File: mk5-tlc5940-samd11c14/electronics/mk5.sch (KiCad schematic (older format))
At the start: 47 parts, among them J1 IN/OUT, J10 Conn_01x01, J11 Conn_01x01, J12 Conn_01x01, J13 Conn_01x01, J14 Conn_01x01, J15 Conn_01x01, J16 Conn_01x01, J17 Conn_01x01, J18 Conn_01x01, J19 Conn_01x01, J2 USB, J20 Conn_01x01, J21 Conn_01x01, J22 Conn_01x01, J23 +LED, J24 +LED, J25 +LED, J26 +LED, J27 +LED, J3 OUT15, J4 GS2, J5 BUTTON, J6 +LED, J7 Conn_01x01, J8 Conn_01x01, J9 Conn_01x01, Q1 MOSFET 20V 3A, SW1 BTN, U1 USBLC6-2SC6, U2 MCP1702-3302_SOT23, U3 SAMD11D14A-M, U4 TLC5940PWP

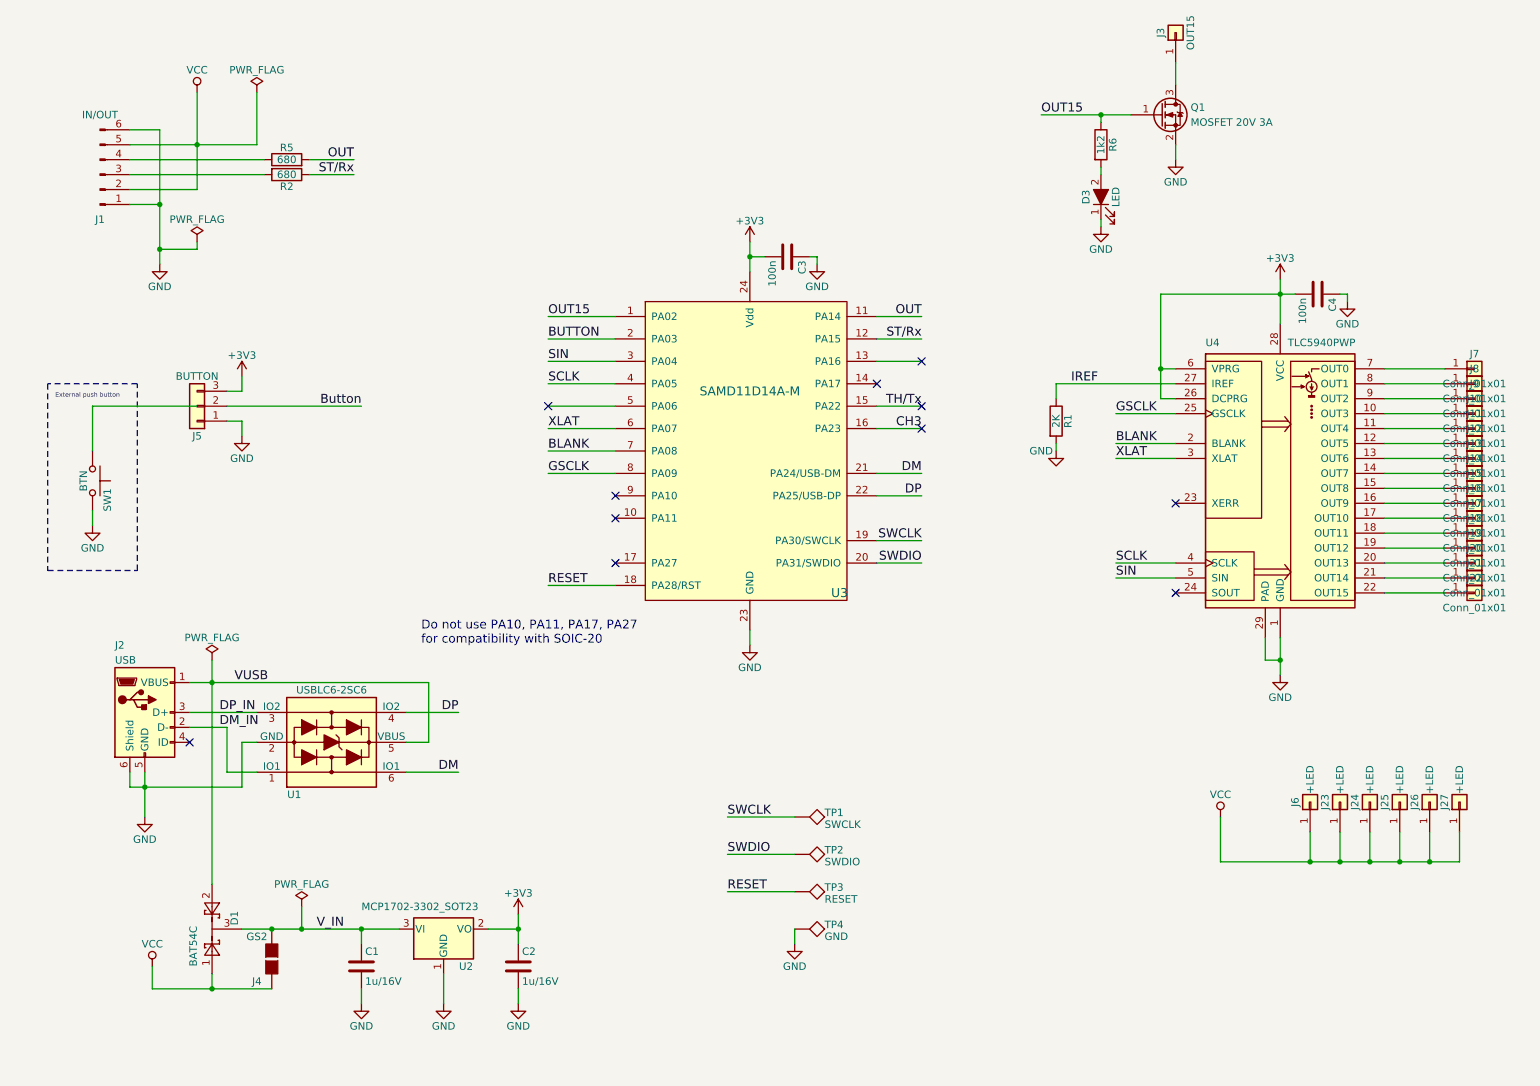
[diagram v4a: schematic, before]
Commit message: Finalize layout with reverse-mount LED
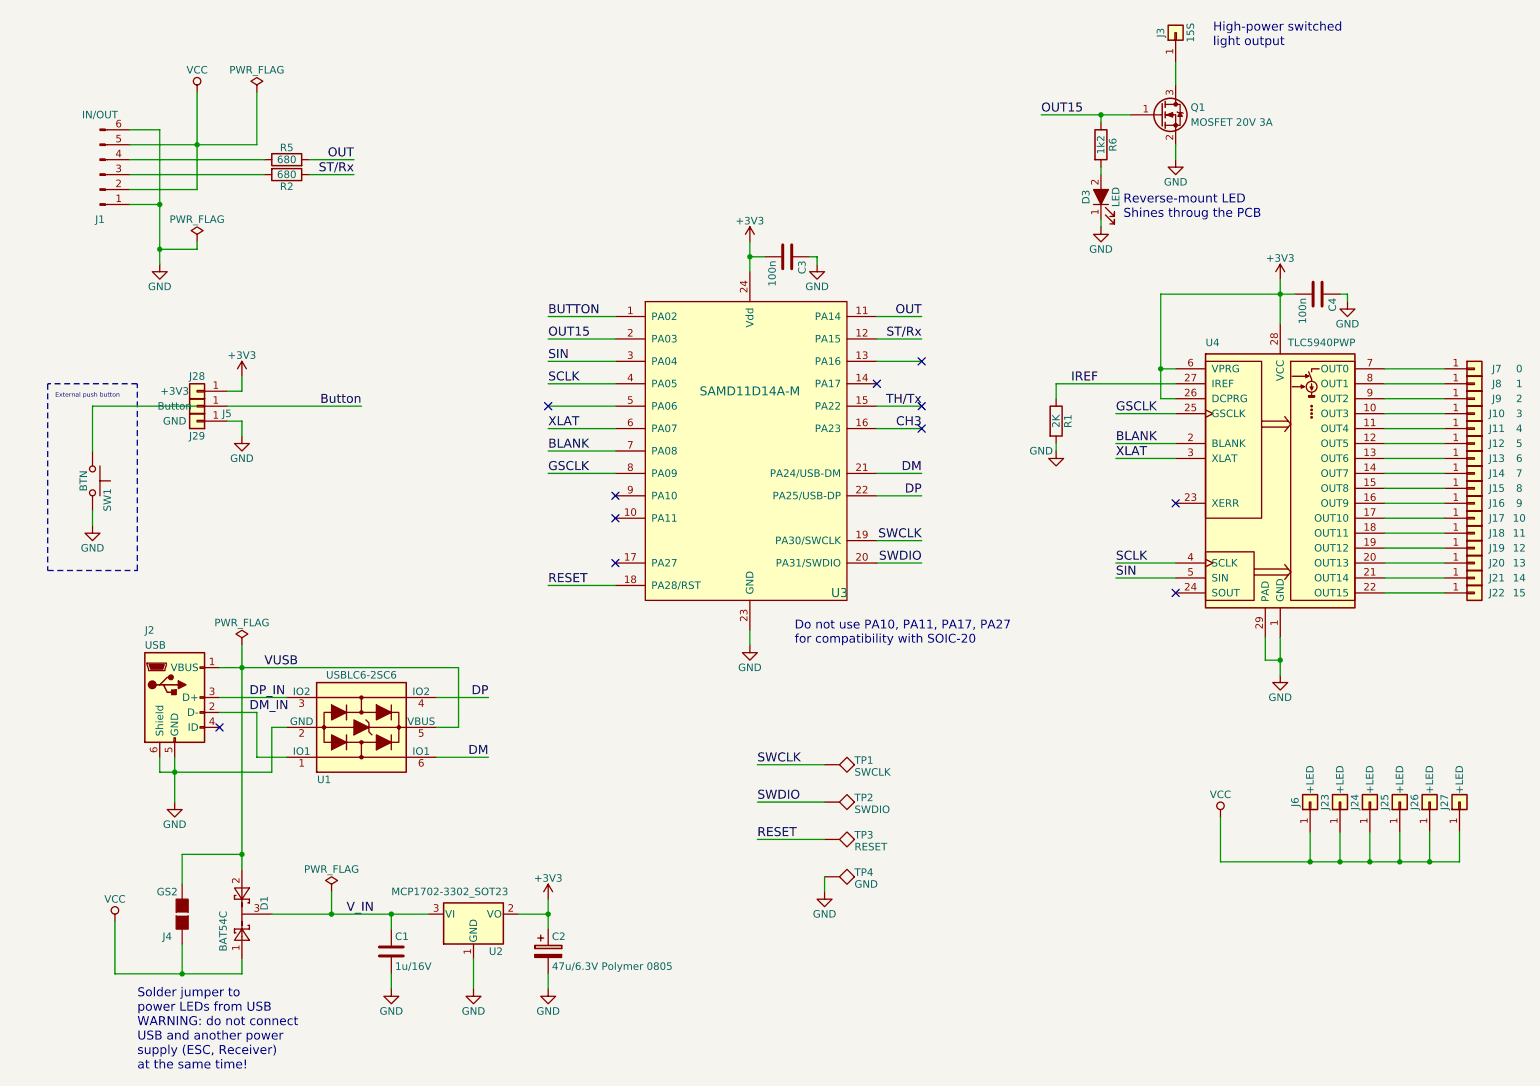
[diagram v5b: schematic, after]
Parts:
- removed C2: 1u/16V, Capacitors_SMD:C_0805, symbol C
- removed J5: BUTTON, Socket_Strips:Socket_Strip_Straight_1x03, symbol Conn_01x03
- added C2: 47u/6.3V Polymer 0805, Capacitors_SMD:C_0805, symbol CP
- added J28: Button, Measurement_Points:Measurement_Point_Round-SMD-Pad_Small, symbol Conn_01x01
- added J29: GND, Measurement_Points:Measurement_Point_Round-SMD-Pad_Small, symbol Conn_01x01
- added J5: +3V3, Measurement_Points:Measurement_Point_Round-SMD-Pad_Small, symbol Conn_01x01
- D3: footprint LEDs:LED_0805_HandSoldering -> Reverse-LED:REVERSE_MOUNT_ROHM_SLM-81
- J10: value Conn_01x01 -> 3
- J11: value Conn_01x01 -> 4
- J12: value Conn_01x01 -> 5
- J13: value Conn_01x01 -> 6
- J14: value Conn_01x01 -> 7
- J15: value Conn_01x01 -> 8
- J16: value Conn_01x01 -> 9
- J17: value Conn_01x01 -> 10
- J18: value Conn_01x01 -> 11
- J19: value Conn_01x01 -> 12
- J20: value Conn_01x01 -> 13
- J21: value Conn_01x01 -> 14
- J22: value Conn_01x01 -> 15
- J3: value OUT15 -> 15S
- J7: value Conn_01x01 -> 0
- J8: value Conn_01x01 -> 1
- J9: value Conn_01x01 -> 2
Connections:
- net +3V3: now also C2.1, J5.1 (Pin_1)
- net BUTTON: now also U3.1 (PA02); no longer U3.2 (PA03)
- net Button: now also J28.1 (Pin_1)
- net GND: now also C2.2, J29.1 (Pin_1)
- net OUT15: now also U3.2 (PA03); no longer U3.1 (PA02)
- net VUSB: now also J4.2 (G2)
- net V_IN: no longer J4.2 (G2)
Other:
- note added: "High-power switched\nlight output"
- note added: "Reverse-mount LED\nShines throug the PCB"
- note added: "Solder jumper to\npower LEDs from USB\nWARNING: do not connect\nUSB and another power \nsupply (ESC, Receiver) \nat the same time!"
- moved on the sheet: C1, D1, J2, J4, TP1, TP2, TP3, TP4, U1, U2

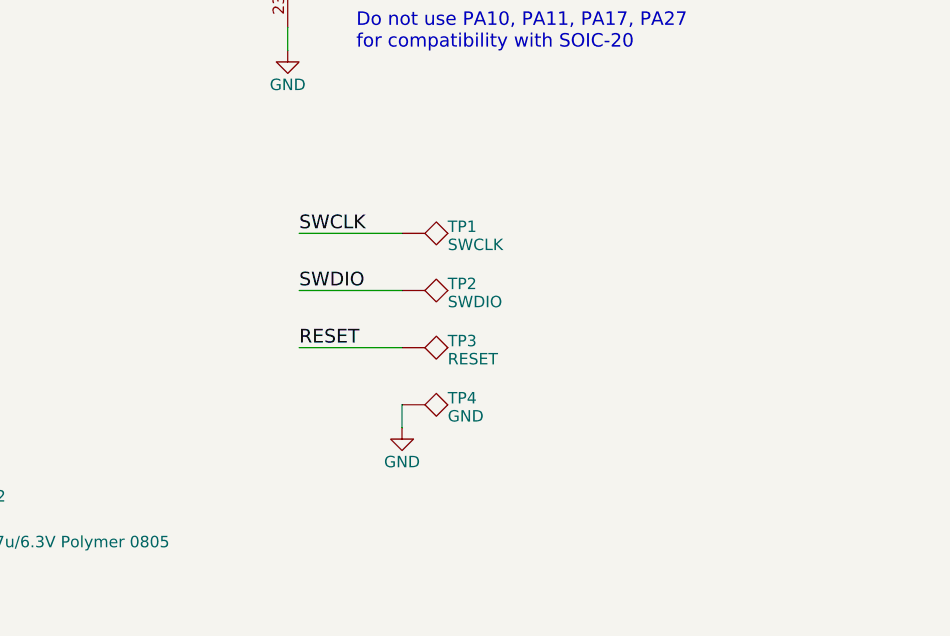
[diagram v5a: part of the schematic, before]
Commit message: Add test points
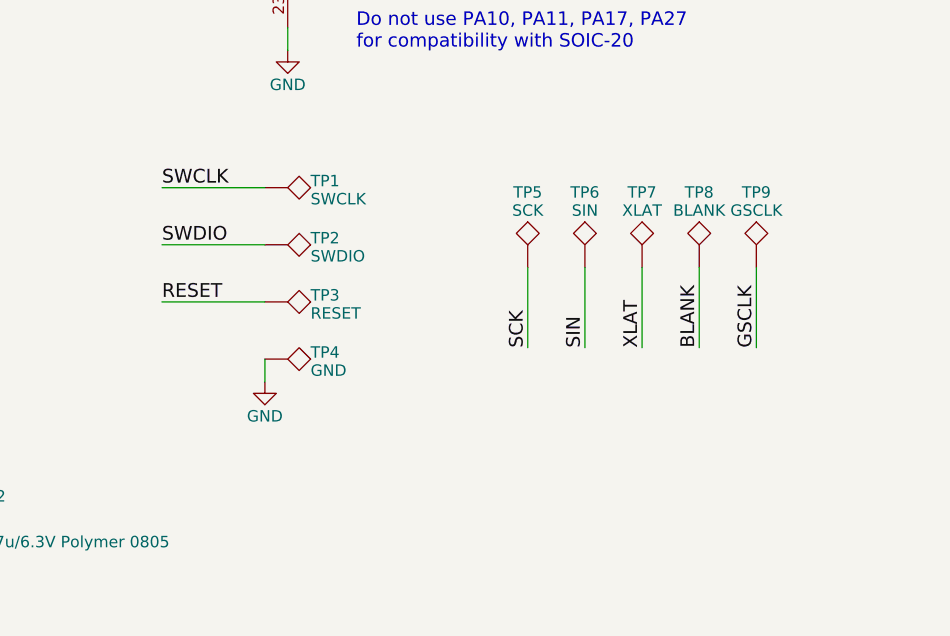
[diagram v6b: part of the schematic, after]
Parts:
- added TP5: SCK, SMD-pads:Measurement_Point_Round-SMD-Pad_1mm, symbol TEST
- added TP6: SIN, SMD-pads:Measurement_Point_Round-SMD-Pad_1mm, symbol TEST
- added TP7: XLAT, SMD-pads:Measurement_Point_Round-SMD-Pad_1mm, symbol TEST
- added TP8: BLANK, SMD-pads:Measurement_Point_Round-SMD-Pad_1mm, symbol TEST
- added TP9: GSCLK, SMD-pads:Measurement_Point_Round-SMD-Pad_1mm, symbol TEST
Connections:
- net BLANK: now also TP8.1
- net GSCLK: now also TP9.1
- net SIN: now also TP6.1
- net XLAT: now also TP7.1
- new net SCK: TP5.1
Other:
- moved on the sheet: TP1, TP2, TP3, TP4
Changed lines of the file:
@@
 L TEST TP1
 U 1 1 59C46169
-P 6200 5600
-F 0 "TP1" V 6200 5800 50  0000 L BNN
-F 1 "SWCLK" V 6250 5800 50  0000 L CNN
-F 2 "Measurement_Points:Measurement_Point_Round-SMD-Pad_Small" H 6200 5600 50  0001 C CNN
-F 3 "" H 6200 5600 50  0001 C CNN
-	1    6200 5600
+P 5600 5400
+F 0 "TP1" V 5600 5600 50  0000 L BNN
+F 1 "SWCLK" V 5650 5600 50  0000 L CNN
+F 2 "Measurement_Points:Measurement_Point_Round-SMD-Pad_Small" H 5600 5400 50  0001 C CNN
+F 3 "" H 5600 5400 50  0001 C CNN
+	1    5600 5400
 	0    1    1    0
 $EndComp
@@
 L TEST TP2
 U 1 1 59C46225
-P 6200 5850
-F 0 "TP2" V 6200 6050 50  0000 L BNN
-F 1 "SWDIO" V 6250 6050 50  0000 L CNN
-F 2 "Measurement_Points:Measurement_Point_Round-SMD-Pad_Small" H 6200 5850 50  0001 C CNN
-F 3 "" H 6200 5850 50  0001 C CNN
-	1    6200 5850
+P 5600 5650
+F 0 "TP2" V 5600 5850 50  0000 L BNN
+F 1 "SWDIO" V 5650 5850 50  0000 L CNN
+F 2 "Measurement_Points:Measurement_Point_Round-SMD-Pad_Small" H 5600 5650 50  0001 C CNN
+F 3 "" H 5600 5650 50  0001 C CNN
+	1    5600 5650
 	0    1    1    0
 $EndComp
@@
 L TEST TP3
 U 1 1 59C4652D
-P 6200 6100
-F 0 "TP3" V 6200 6300 50  0000 L BNN
-F 1 "RESET" V 6250 6300 50  0000 L CNN
-F 2 "Measurement_Points:Measurement_Point_Round-SMD-Pad_Small" H 6200 6100 50  0001 C CNN
-F 3 "" H 6200 6100 50  0001 C CNN
-	1    6200 6100
+P 5600 5900
+F 0 "TP3" V 5600 6100 50  0000 L BNN
+F 1 "RESET" V 5650 6100 50  0000 L CNN
+F 2 "Measurement_Points:Measurement_Point_Round-SMD-Pad_Small" H 5600 5900 50  0001 C CNN
+F 3 "" H 5600 5900 50  0001 C CNN
+	1    5600 5900
 	0    1    1    0
 $EndComp
@@
 L TEST TP4
 U 1 1 59DB5CFC
-P 6200 6350
-F 0 "TP4" V 6200 6550 50  0000 L BNN
-F 1 "GND" V 6250 6550 50  0000 L CNN
-F 2 "Measurement_Points:Measurement_Point_Round-SMD-Pad_Small" H 6200 6350 50  0001 C CNN
-F 3 "" H 6200 6350 50  0001 C CNN
-	1    6200 6350
+P 5600 6150
+F 0 "TP4" V 5600 6350 50  0000 L BNN
+F 1 "GND" V 5650 6350 50  0000 L CNN
+F 2 "Measurement_Points:Measurement_Point_Round-SMD-Pad_Small" H 5600 6150 50  0001 C CNN
+F 3 "" H 5600 6150 50  0001 C CNN
+	1    5600 6150
 	0    1    1    0
 $EndComp
@@
 L GND #PWR022
 U 1 1 59DB5EB3
-P 6200 6450
-F 0 "#PWR022" H 6200 6200 50  0001 C CNN
-F 1 "GND" H 6200 6300 50  0000 C CNN
-F 2 "" H 6200 6450 50  0001 C CNN
-F 3 "" H 6200 6450 50  0001 C CNN
-	1    6200 6450
+P 5600 6250
+F 0 "#PWR022" H 5600 6000 50  0001 C CNN
+F 1 "GND" H 5600 6100 50  0000 C CNN
+F 2 "" H 5600 6250 50  0001 C CNN
+F 3 "" H 5600 6250 50  0001 C CNN
+	1    5600 6250
 	1    0    0    -1
 $EndComp
@@
 Text Label 6850 4250 2    60   ~ 0
 SWDIO
-Text Label 5750 5600 0    60   ~ 0
+Text Label 5150 5400 0    60   ~ 0
 SWCLK
-Text Label 5750 5850 0    60   ~ 0
+Text Label 5150 5650 0    60   ~ 0
 SWDIO
-Text Label 5750 6100 0    60   ~ 0
+Text Label 5150 5900 0    60   ~ 0
 RESET
 Text Label 4350 4400 0    60   ~ 0
@@
 Connection ~ 10250 6250
 Wire Wire Line
-	6200 6350 6200 6450
+	5600 6150 5600 6250
 Wire Wire Line
 	1550 1350 1750 1350
@@
 	7750 3050 7750 3150
 Wire Wire Line
-	6200 5600 5750 5600
-Wire Wire Line
-	6200 5850 5750 5850
-Wire Wire Line
-	6200 6100 5750 6100
+	5600 5400 5150 5400
+Wire Wire Line
+	5600 5650 5150 5650
+Wire Wire Line
+	5600 5900 5150 5900
 Wire Wire Line
 	8050 1300 8050 1250
@@
 Text Notes 1600 7650 0    60   ~ 0
 Solder jumper to\npower LEDs from USB\nWARNING: do not connect\nUSB and another power \nsupply (ESC, Receiver) \nat the same time!
+$Comp
+L TEST TP6
+U 1 1 5A12668E
+P 7000 5750
+F 0 "TP6" H 7000 6050 50  0000 C BNN
+F 1 "SIN" H 7000 6000 50  0000 C CNN
+F 2 "SMD-pads:Measurement_Point_Round-SMD-Pad_1mm" H 7000 5750 50  0001 C CNN
+F 3 "" H 7000 5750 50  0001 C CNN
+	1    7000 5750
+	1    0    0    -1
+$EndComp
+$Comp
+L TEST TP7
+U 1 1 5A1272F3
+P 7250 5750
+F 0 "TP7" H 7250 6050 50  0000 C BNN
+F 1 "XLAT" H 7250 6000 50  0000 C CNN
+F 2 "SMD-pads:Measurement_Point_Round-SMD-Pad_1mm" H 7250 5750 50  0001 C CNN
+F 3 "" H 7250 5750 50  0001 C CNN
+	1    7250 5750
+	1    0    0    -1
+$EndComp
+$Comp
+L TEST TP8
+U 1 1 5A1273A0
+P 7500 5750
+F 0 "TP8" H 7500 6050 50  0000 C BNN
+F 1 "BLANK" H 7500 6000 50  0000 C CNN
+F 2 "SMD-pads:Measurement_Point_Round-SMD-Pad_1mm" H 7500 5750 50  0001 C CNN
+F 3 "" H 7500 5750 50  0001 C CNN
+	1    7500 5750
+	1    0    0    -1
+$EndComp
+$Comp
+L TEST TP9
+U 1 1 5A127450
+P 7750 5750
+F 0 "TP9" H 7750 6050 50  0000 C BNN
+F 1 "GSCLK" H 7750 6000 50  0000 C CNN
+F 2 "SMD-pads:Measurement_Point_Round-SMD-Pad_1mm" H 7750 5750 50  0001 C CNN
+F 3 "" H 7750 5750 50  0001 C CNN
+	1    7750 5750
+	1    0    0    -1
+$EndComp
+$Comp
+L TEST TP5
+U 1 1 5A12767F
+P 6750 5750
+F 0 "TP5" H 6750 6050 50  0000 C BNN
+F 1 "SCK" H 6750 6000 50  0000 C CNN
+F 2 "SMD-pads:Measurement_Point_Round-SMD-Pad_1mm" H 6750 5750 50  0001 C CNN
+F 3 "" H 6750 5750 50  0001 C CNN
+	1    6750 5750
+	1    0    0    -1
+$EndComp
+Wire Wire Line
+	6750 5750 6750 6100
+Wire Wire Line
+	7000 5750 7000 6100
+Wire Wire Line
+	7250 5750 7250 6100
+Wire Wire Line
+	7500 5750 7500 6100
+Wire Wire Line
+	7750 5750 7750 6100
+Text Label 6750 6100 1    60   ~ 0
+SCK
+Text Label 7000 6100 1    60   ~ 0
+SIN
+Text Label 7250 6100 1    60   ~ 0
+XLAT
+Text Label 7500 6100 1    60   ~ 0
+BLANK
+Text Label 7750 6100 1    60   ~ 0
+GSCLK
 $EndSCHEMATC

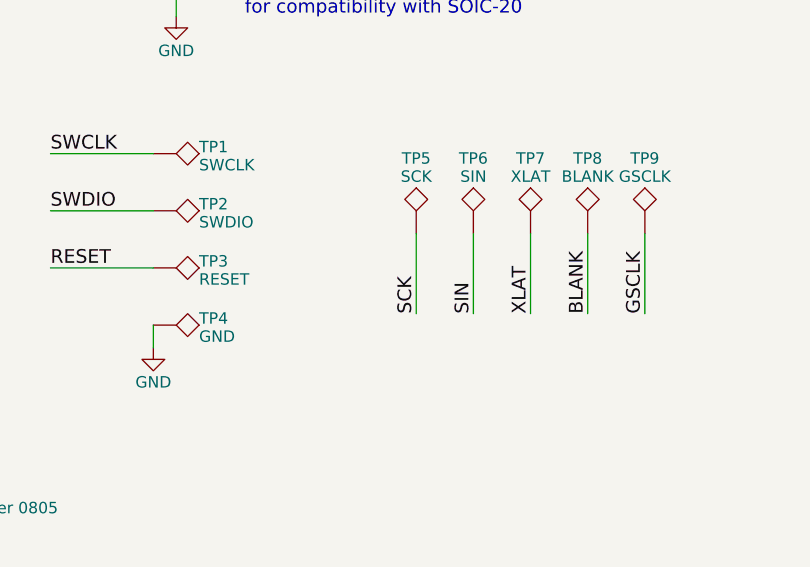
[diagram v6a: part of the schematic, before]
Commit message: Layout test points and tweak
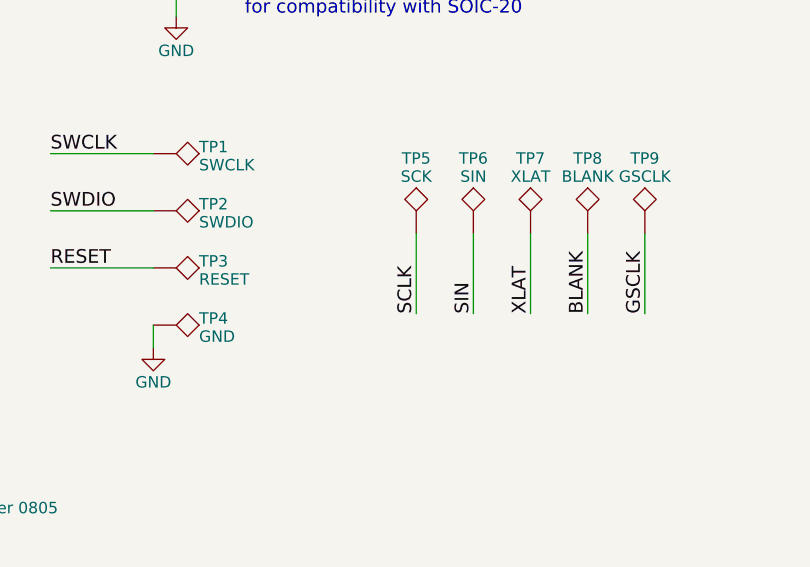
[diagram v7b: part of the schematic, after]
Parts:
- TP5, TP6, TP7, TP8, TP9: footprint SMD-pads:Measurement_Point_Round-SMD-Pad_1mm -> SMD-pads:Measurement_Point_Round-SMD-Pad_0_6mm
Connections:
- net SCK is gone; now on net SCLK: TP5.1
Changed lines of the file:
@@
 F 0 "TP6" H 7000 6050 50  0000 C BNN
 F 1 "SIN" H 7000 6000 50  0000 C CNN
-F 2 "SMD-pads:Measurement_Point_Round-SMD-Pad_1mm" H 7000 5750 50  0001 C CNN
+F 2 "SMD-pads:Measurement_Point_Round-SMD-Pad_0_6mm" H 7000 5750 50  0001 C CNN
 F 3 "" H 7000 5750 50  0001 C CNN
 	1    7000 5750
@@
 F 0 "TP7" H 7250 6050 50  0000 C BNN
 F 1 "XLAT" H 7250 6000 50  0000 C CNN
-F 2 "SMD-pads:Measurement_Point_Round-SMD-Pad_1mm" H 7250 5750 50  0001 C CNN
+F 2 "SMD-pads:Measurement_Point_Round-SMD-Pad_0_6mm" H 7250 5750 50  0001 C CNN
 F 3 "" H 7250 5750 50  0001 C CNN
 	1    7250 5750
@@
 F 0 "TP8" H 7500 6050 50  0000 C BNN
 F 1 "BLANK" H 7500 6000 50  0000 C CNN
-F 2 "SMD-pads:Measurement_Point_Round-SMD-Pad_1mm" H 7500 5750 50  0001 C CNN
+F 2 "SMD-pads:Measurement_Point_Round-SMD-Pad_0_6mm" H 7500 5750 50  0001 C CNN
 F 3 "" H 7500 5750 50  0001 C CNN
 	1    7500 5750
@@
 F 0 "TP9" H 7750 6050 50  0000 C BNN
 F 1 "GSCLK" H 7750 6000 50  0000 C CNN
-F 2 "SMD-pads:Measurement_Point_Round-SMD-Pad_1mm" H 7750 5750 50  0001 C CNN
+F 2 "SMD-pads:Measurement_Point_Round-SMD-Pad_0_6mm" H 7750 5750 50  0001 C CNN
 F 3 "" H 7750 5750 50  0001 C CNN
 	1    7750 5750
@@
 F 0 "TP5" H 6750 6050 50  0000 C BNN
 F 1 "SCK" H 6750 6000 50  0000 C CNN
-F 2 "SMD-pads:Measurement_Point_Round-SMD-Pad_1mm" H 6750 5750 50  0001 C CNN
+F 2 "SMD-pads:Measurement_Point_Round-SMD-Pad_0_6mm" H 6750 5750 50  0001 C CNN
 F 3 "" H 6750 5750 50  0001 C CNN
 	1    6750 5750
@@
 	7750 5750 7750 6100
 Text Label 6750 6100 1    60   ~ 0
-SCK
+SCLK
 Text Label 7000 6100 1    60   ~ 0
 SIN

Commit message: Add solder paste to heatsink pad of TLC5940
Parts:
- U4: footprint Housings_SSOP:HTSSOP-28_4.4x9.7mm_Pitch0.65mm_ThermalPad -> Housings_SSOP_modified:HTSSOP-28_4.4x9.7mm_Pitch0.65mm_ThermalPad_paste
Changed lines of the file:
@@
 F 0 "U4" H 8750 4525 50  0000 L CNN
 F 1 "TLC5940PWP" H 9300 4525 50  0000 L CNN
-F 2 "Housings_SSOP:HTSSOP-28_4.4x9.7mm_Pitch0.65mm_ThermalPad" H 9275 2675 50  0001 L CNN
+F 2 "Housings_SSOP_modified:HTSSOP-28_4.4x9.7mm_Pitch0.65mm_ThermalPad_paste" H 9275 2675 50  0001 L CNN
 F 3 "" H 8850 4350 50  0001 C CNN
 	1    9250 3650
